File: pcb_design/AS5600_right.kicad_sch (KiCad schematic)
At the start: 5 parts, among them IC2 AS5600-ASOT, J5 AS5600_Right

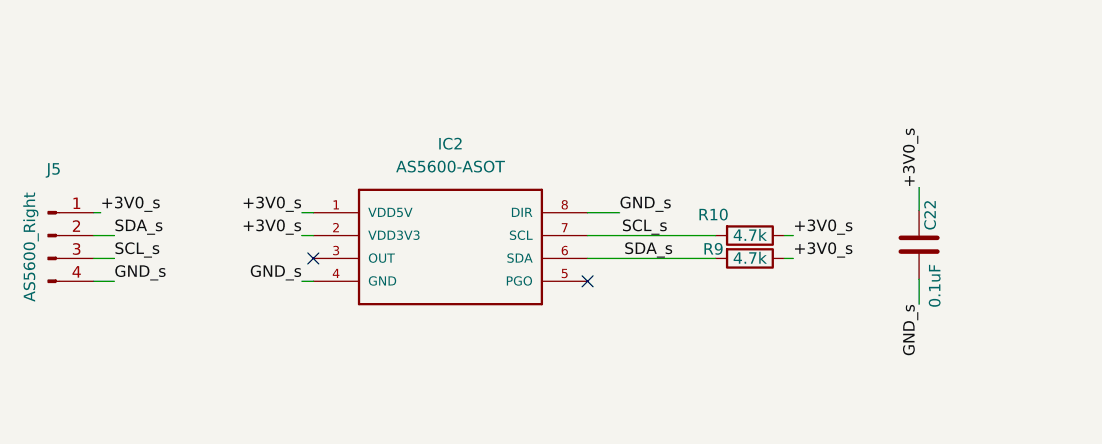
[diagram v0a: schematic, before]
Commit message: changed AS5600 to AS5048B
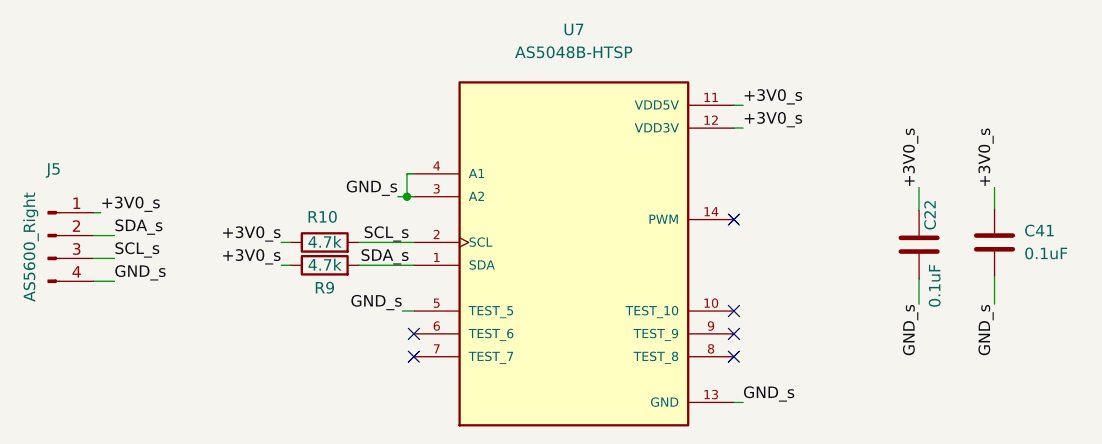
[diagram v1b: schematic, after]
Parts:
- removed IC2: AS5600-ASOT, AS5600-ASOT:SOIC127P600X175-8N, symbol AS5600-ASOT:AS5600-ASOT
- added C41: 0.1uF, Capacitor_SMD:C_0402_1005Metric, symbol Device:C
- added U7: AS5048B-HTSP, AS5048B-HTSP:SOP65P640X120-14N, symbol AS5048B-HTSP:AS5048B-HTSP
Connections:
- net +3V0_s: now also C41.1, U7.11 (VDD5V), U7.12 (VDD3V)
- net GND_s: now also C41.2, U7.13 (GND), U7.3 (A2), U7.4 (A1), U7.5 (TEST_5)
- net SCL_s: now also R10.2, U7.2 (SCL); no longer R9.2
- net SDA_s: now also R9.2, U7.1 (SDA); no longer R10.2
- no-connect marks 2 -> 6
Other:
- moved on the sheet: R10, R9
